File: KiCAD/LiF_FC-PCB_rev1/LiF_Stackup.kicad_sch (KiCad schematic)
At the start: 3 parts, among them J45 Conn_01x10_Socket, J47 Conn_01x16_Pin, J48 Conn_01x16_Pin

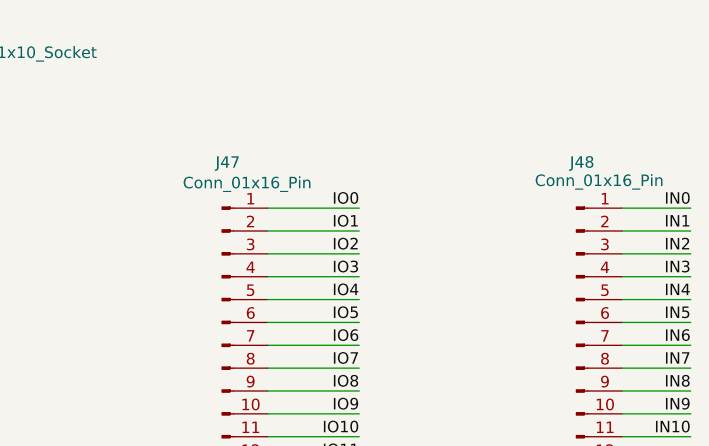
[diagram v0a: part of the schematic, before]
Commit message: backup before redoing the analog section
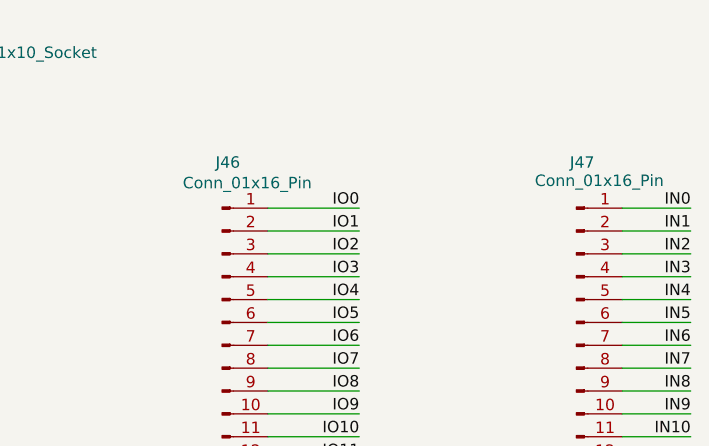
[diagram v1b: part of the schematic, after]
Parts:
- renumbered J47 to J46, J48 to J47
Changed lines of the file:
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@@
 		(on_board yes)
 		(dnp no)
-		(property "Reference" "J47"
+		(property "Reference" "J46"
 			(at 76.835 72.39 0)
 			(effects
@@
 			(project "LiF_FC-PCB_rev1"
 				(path "/9e3e8da7-e506-46c9-90e5-307e4ad30d29/430b22f5-fe40-4c7c-a3d7-4ca49b0a1260"
-					(reference "J47")
+					(reference "J46")
 					(unit 1)
 				)
@@
 		(on_board yes)
 		(dnp no)
-		(property "Reference" "J48"
+		(property "Reference" "J47"
 			(at 116.205 72.39 0)
 			(effects
@@
 			(project "LiF_FC-PCB_rev1"
 				(path "/9e3e8da7-e506-46c9-90e5-307e4ad30d29/430b22f5-fe40-4c7c-a3d7-4ca49b0a1260"
-					(reference "J48")
+					(reference "J47")
 					(unit 1)
 				)

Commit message: progress save for the night. landmarking of service PCB is almost done. redid the analog section layout to make it more assembleable and better utilze the space. Still need to do ACC, R3V3, IO, test points, and jumpers
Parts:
- J47: footprint Connector_PinHeader_2.54mm:PinHeader_1x16_P2.54mm_Vertical -> Connector_PinHeader_2.54mm:PinHeader_1x19_P2.54mm_Vertical; symbol Connector:Conn_01x16_Pin -> Connector:Conn_01x19_Pin
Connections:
- net IO16: now reaches J47.12 (Pin_12)
- net IO17: now reaches J47.13 (Pin_13)
- net IO18: now reaches J47.14 (Pin_14)
- net IO19: now reaches J47.15 (Pin_15)
- net IO20: now reaches J47.16 (Pin_16)
- new net IO21: J47.17 (Pin_17)
- new net IO22: J47.18 (Pin_18)
- new net IO23: J47.19 (Pin_19)

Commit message: routing in progress. backup save
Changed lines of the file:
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@@
 		)
 	)
-	(hierarchical_label "IO[16..22]"
+	(hierarchical_label "IO[16..23]"
 		(shape bidirectional)
 		(at 93.98 132.08 180)

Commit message: finished service PCB routing and silkscreen, finished IO PCB layout, routing, and silkscreen. Exported production files, submitted PCB for manufacturing by JLCPCB
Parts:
- J45: value Conn_01x10_Socket -> Top
- J46: value Conn_01x16_Pin -> Left
- J47: value Conn_01x16_Pin -> Right
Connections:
- net 3V3_{IN}: now also J45.4 (Pin_4), J45.5 (Pin_5)
- net 5V0_{IN}: now also J45.6 (Pin_6), J45.7 (Pin_7); no longer J45.1 (Pin_1)
- net GND: now reaches J45.10 (Pin_10)
- net GND: now also J45.1 (Pin_1), J45.2 (Pin_2), J45.3 (Pin_3)
- net V_{supply}: now reaches J45.8 (Pin_8)
- net V_{supply}: now also J45.9 (Pin_9)
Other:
- moved on the sheet: J47
